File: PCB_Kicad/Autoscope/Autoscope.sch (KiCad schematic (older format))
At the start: 40 parts

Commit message: update sch & create pcb
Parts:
- removed C?: 100nF, symbol Device:C_Small
- removed J?: Conn_02x03_Odd_Even, symbol Connector_Generic:Conn_02x03_Odd_Even
- J1, J2, J3, J4, J5: renamed from J?; footprint (none) -> Connector_PinHeader_2.54mm:PinHeader_1x02_P2.54mm_Horizontal
- J10, J11, J12: renamed from J?; footprint (none) -> Connector_PinHeader_2.54mm:PinHeader_2x02_P2.54mm_Horizontal
- J6: renamed from J?; footprint (none) -> Autoscope:PJ-043H
- J7: renamed from J?; footprint (none) -> Connector_PinHeader_2.54mm:PinHeader_1x04_P2.54mm_Horizontal
- J8: renamed from J?; footprint (none) -> Connector_PinSocket_2.54mm:PinSocket_2x20_P2.54mm_Vertical
- J9: renamed from J?; footprint (none) -> Connector_PinHeader_2.54mm:PinHeader_1x05_P2.54mm_Horizontal
- U1: renamed from U?; footprint (none) -> Autoscope:R-78B-2.0
- gave numbers to parts that had none: 25
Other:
- moved on the sheet: C6, C7, J7, J9

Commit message: schematic ok & pcb in progress
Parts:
- removed J10, J11, J12: Conn_01x04, Connector_PinHeader_2.54mm:PinHeader_2x02_P2.54mm_Horizontal, symbol Connector_Generic:Conn_01x04
- added F1: 3A, Autoscope:Fuseholder5x20_horiz_SemiClosed_Casing10x25mm, symbol Device:Fuse
- added J10, J11, J12: Conn_02x02_Odd_Even, Connector_PinHeader_2.54mm:PinHeader_2x02_P2.54mm_Horizontal, symbol Connector_Generic:Conn_02x02_Odd_Even
- C1, C12, C13, C14, C2, C3, C4, C5, C6, C7, C8: footprint (none) -> Capacitor_SMD:C_0805_2012Metric_Pad1.15x1.40mm_HandSolder
- C10, C11, C9: footprint (none) -> Capacitor_Tantalum_SMD:CP_EIA-7343-43_Kemet-X_Pad2.25x2.55mm_HandSolder
- D1: value D_Schottky_ALT -> Schottky; footprint (none) -> Diode_SMD:D_SMC_Handsoldering
- D2: footprint (none) -> Diode_SMD:D_SMC_Handsoldering
- R1, R2, R3, R4, R5: footprint (none) -> Resistor_SMD:R_0805_2012Metric_Pad1.15x1.40mm_HandSolder
- SW1: footprint (none) -> Connector_PinHeader_2.54mm:PinHeader_1x02_P2.54mm_Horizontal
- U2, U3, U4: footprint (none) -> Autoscope:A4988
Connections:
- net Posotion_sensor_5 is gone; now on net Position_sensor_5: J8.16 (Pin_16)
- net +12V: now also F1.1; no longer D1.1 (K), D2.1 (K)
- net GPS_EN: now also J8.10 (Pin_10); no longer J8.12 (Pin_12)
- net GPS_Rx: now also J8.7 (Pin_7); no longer J8.8 (Pin_8)
- net GPS_Tx: now also J8.8 (Pin_8); no longer J8.10 (Pin_10)
- net Position_sensor_1: now also J8.11 (Pin_11); no longer J8.7 (Pin_7)
- net Position_sensor_2: now also J8.12 (Pin_12); no longer J8.11 (Pin_11)
- net at D1.2 (A): now also SW1.1 (A); no longer SW1.2 (B)
- net at J6.1 (Pin_1): now also SW1.2 (B); no longer SW1.1 (A)
- net Motor2_1B: now reaches U4.11 (1B)
- net Motor2_1B: now also J11.3 (Pin_3)
- net Motor2_1A: now reaches U4.12 (1A)
- net Motor2_1A: now also J11.4 (Pin_4)
- net Motor2_2A: now reaches U4.13 (2A)
- net Motor2_2A: now also J11.2 (Pin_2)
- net Motor2_2B: now reaches U4.14 (2B)
- net Motor2_2B: now also J11.1 (Pin_1)
- net Motor3_1B: now reaches U3.11 (1B)
- net Motor3_1B: now also J12.3 (Pin_3)
- net Motor3_1A: now reaches U3.12 (1A)
- net Motor3_1A: now also J12.4 (Pin_4)
- net Motor3_2A: now reaches U3.13 (2A)
- net Motor3_2A: now also J12.2 (Pin_2)
- net Motor3_2B: now reaches U3.14 (2B)
- net Motor3_2B: now also J12.1 (Pin_1)
- net Motor1_1B: now reaches U2.11 (1B)
- net Motor1_1B: now also J10.3 (Pin_3)
- net Motor1_1A: now reaches U2.12 (1A)
- net Motor1_1A: now also J10.4 (Pin_4)
- net Motor1_2A: now reaches U2.13 (2A)
- net Motor1_2A: now also J10.2 (Pin_2)
- net Motor1_2B: now reaches U2.14 (2B)
- net Motor1_2B: now also J10.1 (Pin_1)
- new net: D1.1 (K), D2.1 (K), F1.2
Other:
- moved on the sheet: C12, C9, SW1, U3, U4

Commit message: nearly finished pcb
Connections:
- net Motor1_DIR: now also J8.23 (Pin_23); no longer J8.18 (Pin_18)
- net Motor1_EN: now also J8.18 (Pin_18); no longer J8.24 (Pin_24)
- net Motor1_MS1: now also J8.22 (Pin_22); no longer J8.23 (Pin_23)
- net Motor1_MS2: now also J8.24 (Pin_24); no longer J8.22 (Pin_22)
- net Motor1_MS3: now also J8.19 (Pin_19); no longer J8.21 (Pin_21)
- net Motor1_STEP: now also J8.21 (Pin_21); no longer J8.19 (Pin_19)
- net Motor2_DIR: now also J8.31 (Pin_31); no longer J8.26 (Pin_26)
- net Motor2_EN: now also J8.26 (Pin_26); no longer J8.32 (Pin_32)
- net Motor2_MS1: now also J8.27 (Pin_27); no longer J8.31 (Pin_31)
- net Motor2_MS2: now also J8.28 (Pin_28); no longer J8.29 (Pin_29)
- net Motor2_MS3: now also J8.29 (Pin_29); no longer J8.28 (Pin_28)
- net Motor2_STEP: now also J8.32 (Pin_32); no longer J8.27 (Pin_27)
- net Motor3_DIR: now also J8.40 (Pin_40); no longer J8.33 (Pin_33)
- net Motor3_EN: now also J8.37 (Pin_37); no longer J8.40 (Pin_40)
- net Motor3_MS1: now also J8.35 (Pin_35); no longer J8.38 (Pin_38)
- net Motor3_MS2: now also J8.33 (Pin_33); no longer J8.35 (Pin_35)
- net Motor3_MS3: now also J8.36 (Pin_36); no longer J8.37 (Pin_37)
- net Motor3_STEP: now also J8.38 (Pin_38); no longer J8.36 (Pin_36)
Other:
- note added: "GPS"
- note added: "IMU"
- note added: "Motors controllers"
- note added: "Position sensors"
- note added: "Raspberry Pi"
- note added: "Supply"
- moved on the sheet: C1, C2, C3, C4, C5, C7, C8, J1, J2, J3, J4, J5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

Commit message: add BOM
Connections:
- net +3V3: no longer J8.17 (Pin_17)
- no-connect marks 0 -> 1
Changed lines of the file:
@@
 	1    0    0    -1
 $EndComp
-Wire Wire Line
-	4450 2950 4700 2950
-Wire Wire Line
-	4700 2950 4700 3750
-Wire Wire Line
-	4700 3750 4800 3750
-Connection ~ 4700 2950
-Wire Wire Line
-	4700 2950 4800 2950
 $Comp
 L Connector_Generic:Conn_01x02 J1
@@
 Text Notes 2750 600  2    50   ~ 10
 Position sensors
+Wire Wire Line
+	4450 2950 4800 2950
+NoConn ~ 4800 3750
 $EndSCHEMATC

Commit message: finalize PCB files
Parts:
- J6: value Conn_01x02 -> 12VDC Supply
- SW1: value SW_SPST -> Conn_01x02
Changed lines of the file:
@@
 P 4000 1350
 F 0 "SW1" H 4000 1585 50  0000 C CNN
-F 1 "SW_SPST" H 4000 1494 50  0000 C CNN
+F 1 "Conn_01x02" H 4000 1494 50  0000 C CNN
 F 2 "Connector_PinHeader_2.54mm:PinHeader_1x02_P2.54mm_Horizontal" H 4000 1350 50  0001 C CNN
 F 3 "" H 4000 1350 50  0001 C CNN
@@
 P 3250 1350
 F 0 "J6" H 3170 1567 50  0000 C CNN
-F 1 "Conn_01x02" H 3170 1476 50  0000 C CNN
+F 1 "12VDC Supply" H 3170 1476 50  0000 C CNN
 F 2 "Autoscope:PJ-043H" H 3250 1350 50  0001 C CNN
 F 3 "~" H 3250 1350 50  0001 C CNN

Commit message: ready to print PCB
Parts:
- added C15: 100µF, Capacitor_Tantalum_SMD:CP_EIA-7343-43_Kemet-X_Pad2.25x2.55mm_HandSolder, symbol Device:CP1
- added J13: Conn_01x02, Connector_PinHeader_2.54mm:PinHeader_1x02_P2.54mm_Horizontal, symbol Connector_Generic:Conn_01x02
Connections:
- net +12V: now also C15.1, J13.1 (Pin_1)
- net GND: now also C15.2, J13.2 (Pin_2)
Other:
- note added: "Fan supply"
- moved on the sheet: C6, C7, C8, J7, J8, J9

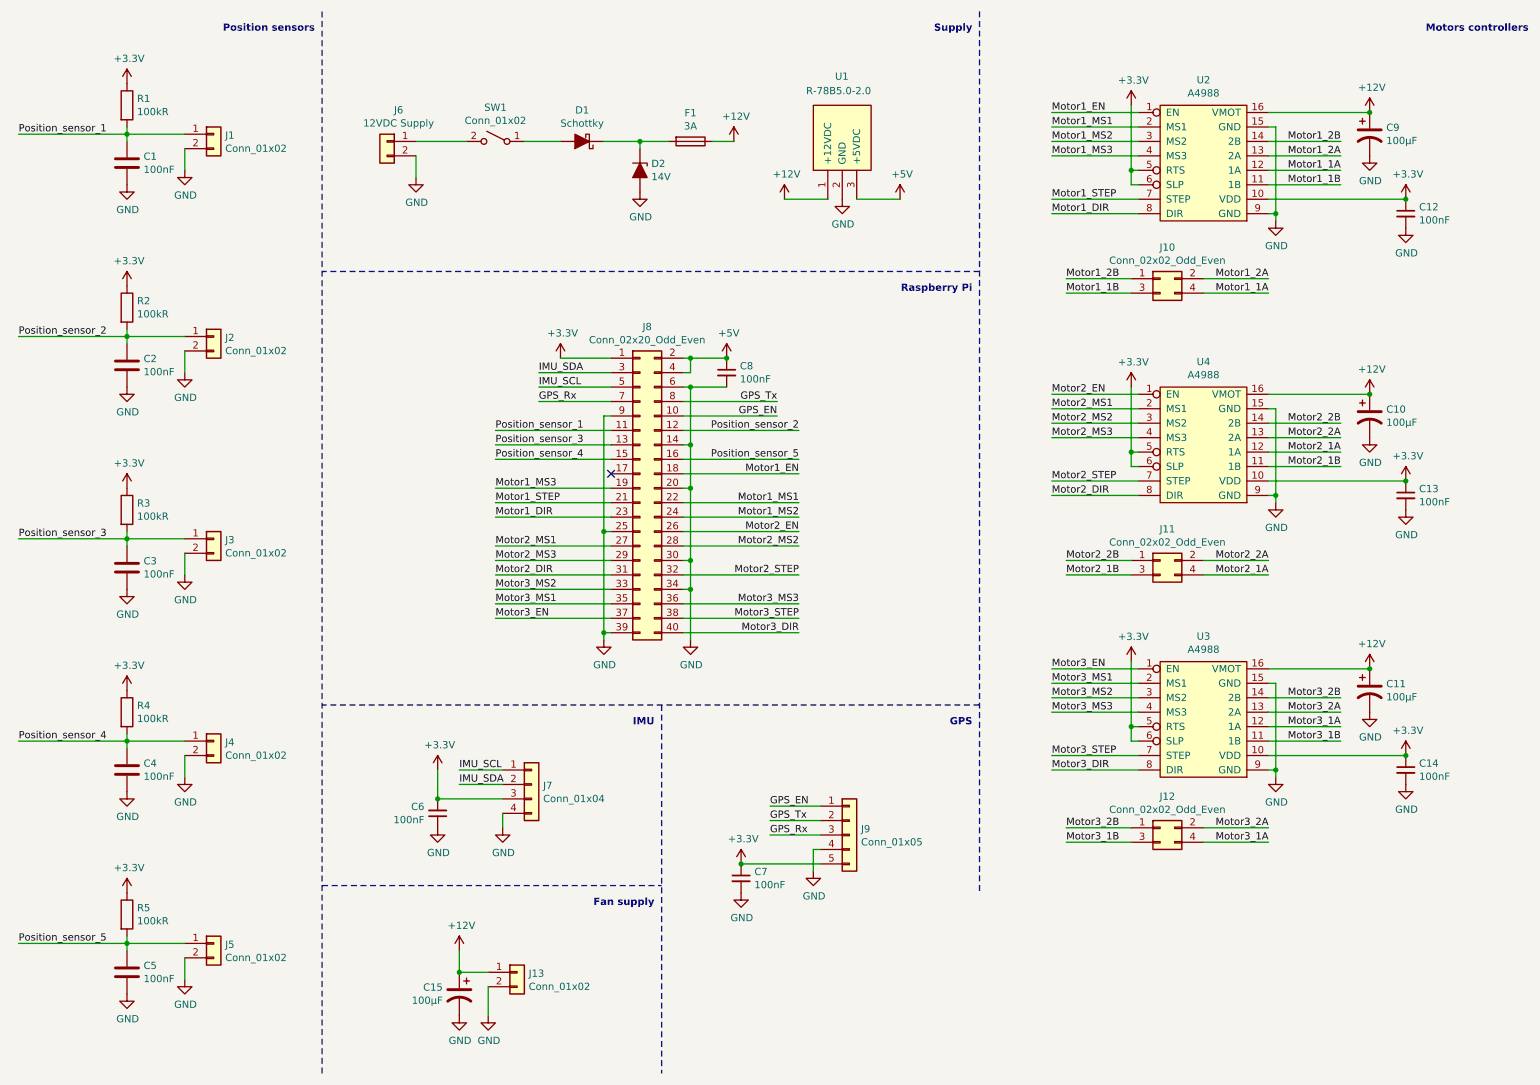
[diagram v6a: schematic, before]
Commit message: refactor labels & fix a bug : invert GPS_EN GPS_Rx
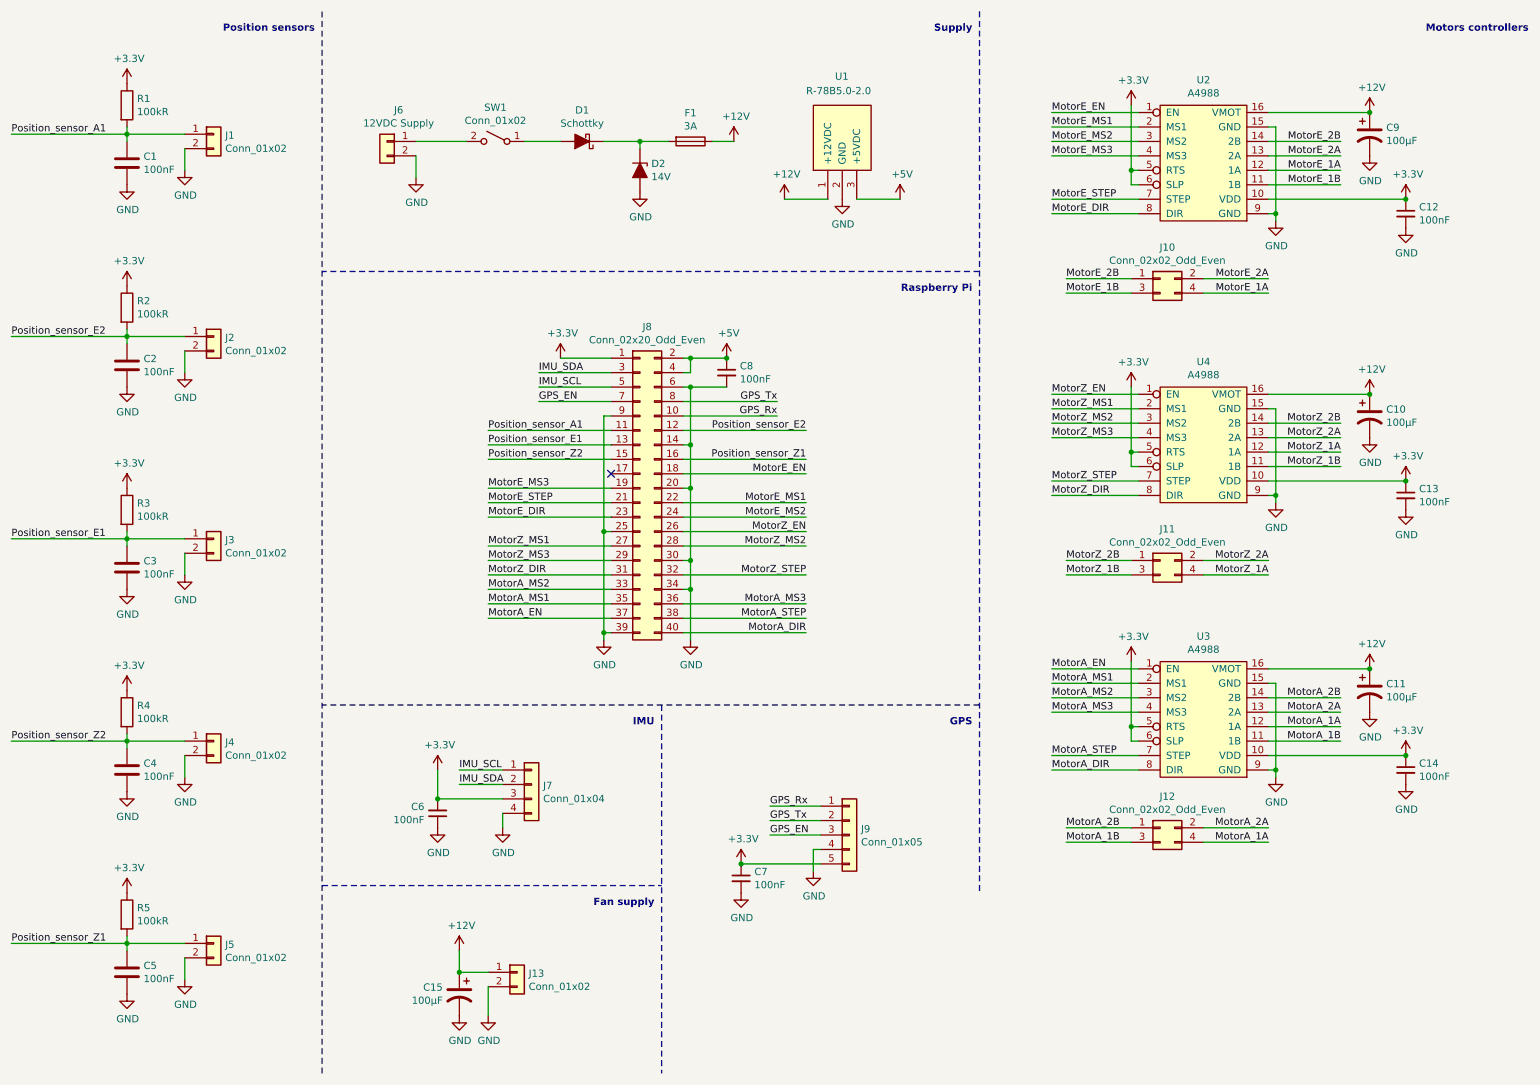
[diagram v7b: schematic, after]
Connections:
- net GPS_EN: now also J8.7 (Pin_7), J9.3 (Pin_3); no longer J8.10 (Pin_10), J9.1 (Pin_1)
- net GPS_Rx: now also J8.10 (Pin_10), J9.1 (Pin_1); no longer J8.7 (Pin_7), J9.3 (Pin_3)
- net Motor1_1A renamed MotorE_1A
- net Motor1_1B renamed MotorE_1B
- net Motor1_2A renamed MotorE_2A
- net Motor1_2B renamed MotorE_2B
- net Motor1_DIR renamed MotorE_DIR
- net Motor1_EN renamed MotorE_EN
- net Motor1_MS1 renamed MotorE_MS1
- net Motor1_MS2 renamed MotorE_MS2
- net Motor1_MS3 renamed MotorE_MS3
- net Motor1_STEP renamed MotorE_STEP
- net Motor2_1A renamed MotorZ_1A
- net Motor2_1B renamed MotorZ_1B
- net Motor2_2A renamed MotorZ_2A
- net Motor2_2B renamed MotorZ_2B
- net Motor2_DIR renamed MotorZ_DIR
- net Motor2_EN renamed MotorZ_EN
- net Motor2_MS1 renamed MotorZ_MS1
- net Motor2_MS2 renamed MotorZ_MS2
- net Motor2_MS3 renamed MotorZ_MS3
- net Motor2_STEP renamed MotorZ_STEP
- net Motor3_1A renamed MotorA_1A
- net Motor3_1B renamed MotorA_1B
- net Motor3_2A renamed MotorA_2A
- net Motor3_2B renamed MotorA_2B
- net Motor3_DIR renamed MotorA_DIR
- net Motor3_EN renamed MotorA_EN
- net Motor3_MS1 renamed MotorA_MS1
- net Motor3_MS2 renamed MotorA_MS2
- net Motor3_MS3 renamed MotorA_MS3
- net Motor3_STEP renamed MotorA_STEP
- net Position_sensor_1 renamed Position_sensor_A1
- net Position_sensor_2 renamed Position_sensor_E2
- net Position_sensor_3 renamed Position_sensor_E1
- net Position_sensor_4 renamed Position_sensor_Z2
- net Position_sensor_5 renamed Position_sensor_Z1
